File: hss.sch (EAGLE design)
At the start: 7 parts, among them IC1 MEGA88-P

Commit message: Third iteration of APM adapter
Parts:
- removed SV2: (no value), con-lstb:MA03-1
- added APM, RADIO: (no value), con-lstb:MA04-1
- added IN, OUT: MCS08, solpad:MCS08
- added Q1: BUZ71, transistor-fet:BUZ71
- C1: device rcl:C-EU050-025X075 -> resistor:C-EUC1206
- IC1: value MEGA88-P -> MEGA328P; device atmel:MEGA8-P -> atmel:MEGA8-AI
- R1, R2: value 120 -> 3k; device rcl:R-EU_0204/7 -> resistor:R-EU_M1206
- renumbered SV1 to HITEC
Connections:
- removed net N$2: IC1.PD0(RXD), SV2.1
- removed net N$6: IC1.PB2(SS/OC1B), SV2.2
- new net N$10: IC1.PB0(ICP), Q1.G
- new net N$11: IN.MP, Q1.S
- new net N$14: APM.3, IC1.PD1(TXD), RADIO.3
- new net N$15: APM.4, IC1.PD0(RXD), RADIO.4
- net GND: now also APM.1, RADIO.1; no longer SV2.3
- net N$3: now also HITEC.2
- net N$4: now also R2.1
- net N$5: now also OUT.MP, Q1.D; no longer HITEC.2, R2.1
- net VCC: now also APM.2, RADIO.2
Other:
- note removed: "Chip Select (SS)"
- moved on the sheet: C1, R1, R2

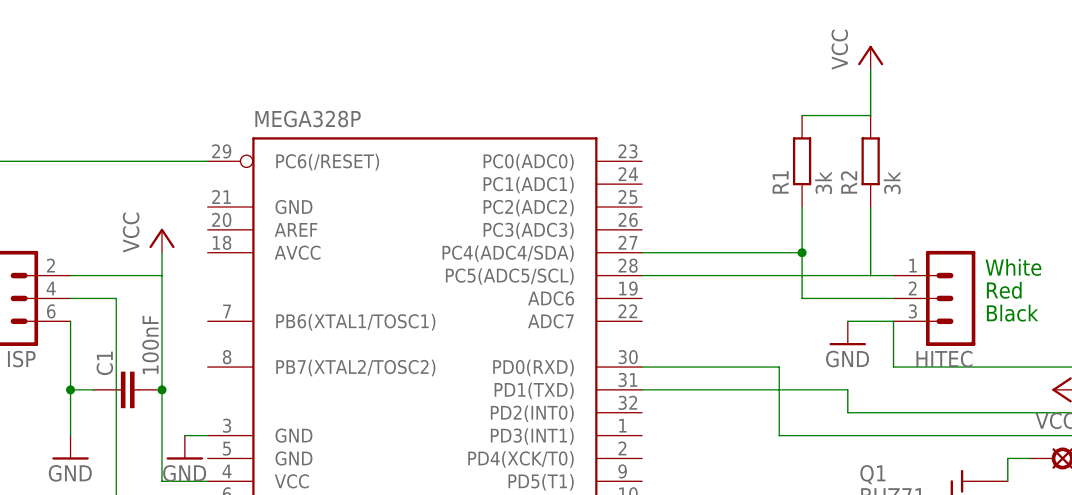
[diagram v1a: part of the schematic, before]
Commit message: Corrected schematic & board
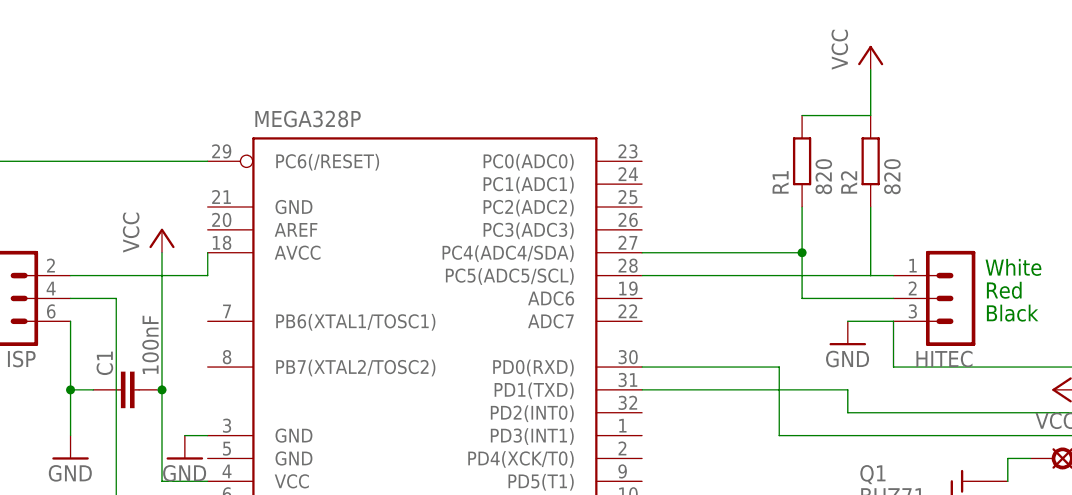
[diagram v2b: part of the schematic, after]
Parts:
- R1, R2: value 3k -> 820
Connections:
- net VCC: now also IC1.AVCC
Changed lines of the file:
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@@
 <?xml version="1.0" encoding="utf-8"?>
 <!DOCTYPE eagle SYSTEM "eagle.dtd">
-<eagle version="6.4">
+<eagle version="6.1">
 <drawing>
 <settings>
@@
 <part name="GND2" library="supply1" deviceset="GND" device=""/>
 <part name="C1" library="resistor" deviceset="C-EU" device="C1206" value="100nF"/>
-<part name="R1" library="resistor" deviceset="R-EU_" device="M1206" value="3k"/>
-<part name="R2" library="resistor" deviceset="R-EU_" device="M1206" value="3k"/>
+<part name="R1" library="resistor" deviceset="R-EU_" device="M1206" value="820"/>
+<part name="R2" library="resistor" deviceset="R-EU_" device="M1206" value="820"/>
 <part name="GND3" library="supply1" deviceset="GND" device=""/>
 <part name="P+1" library="supply1" deviceset="VCC" device=""/>
@@
 <pinref part="C1" gate="G$1" pin="2"/>
 <junction x="40.64" y="55.88"/>
+<pinref part="IC1" gate="G$1" pin="AVCC"/>
+<wire x1="40.64" y1="68.58" x2="45.72" y2="68.58" width="0.1524" layer="91"/>
+<wire x1="45.72" y1="68.58" x2="45.72" y2="71.12" width="0.1524" layer="91"/>
 </segment>
 <segment>

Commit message: version 4 of the board
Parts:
- removed IN, OUT: MCS08, solpad:MCS08
- removed ISP: (no value), con-lstb:MA03-2
- removed Q1: BUZ71, transistor-fet:BUZ71
- removed RADIO: (no value), con-lstb:MA04-1
- added C2: 100nF, resistor:C-EUC1206
- added LED1: GREEN, led:LEDSMT1206
- added LED2: RED, led:LEDSMT1206
- added R3: 68, resistor:R-EU_M1206
- added R4: 150, resistor:R-EU_M1206
- added R5: 10k, resistor:R-EU_M1206
- APM: device con-lstb:MA04-1 -> con-lstb:MA06-2
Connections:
- removed net N$11: IN.MP, Q1.S
- net GND: now also APM.2, APM.3, APM.4, LED1.C, LED2.C; no longer ISP.6, RADIO.1
- net N$1: now also IC1.PB0(ICP), R3.1; no longer IC1.PC6(/RESET), ISP.5
- net N$10: now also APM.11, APM.12, C2.1; no longer IC1.PB0(ICP), Q1.G
- net N$14: now also APM.10, APM.9; no longer APM.3, RADIO.3
- net N$15: now also APM.7, APM.8; no longer APM.4, RADIO.4
- net N$5: now also C2.2, IC1.PC6(/RESET), R5.1; no longer OUT.MP, Q1.D
- net N$7: now also LED1.A, R3.2; no longer IC1.PB5(SCK), ISP.3
- net N$8: now also IC1.PB1(OC1A), R4.1; no longer IC1.PB4(MISO), ISP.1
- net N$9: now also LED2.A, R4.2; no longer IC1.PB3(MOSI/OC2), ISP.4
- net VCC: now also APM.5, APM.6, R5.2; no longer APM.2, ISP.2, RADIO.2
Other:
- note removed: "Rxd"
